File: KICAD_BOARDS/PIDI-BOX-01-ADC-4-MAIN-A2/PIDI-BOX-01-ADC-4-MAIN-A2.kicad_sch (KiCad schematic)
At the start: 87 parts, among them IC1 HCPL-354-000E, J1 Conn_01x10_Pin, J10 Conn_01x01, J2 Conn_02x03_Odd_Even, J3 Conn_02x02_Odd_Even, J4 Conn_02x01, J5 Conn_02x01, J6 CTB0709_3, J7 CTB0709_3, J8 CTB0709_2, J9 Conn_01x01, Q1 BC808, U1 AMS1117-3.3, U2 ADuM1250, U3 AMS1117CD, U4 ADS1115IDGS

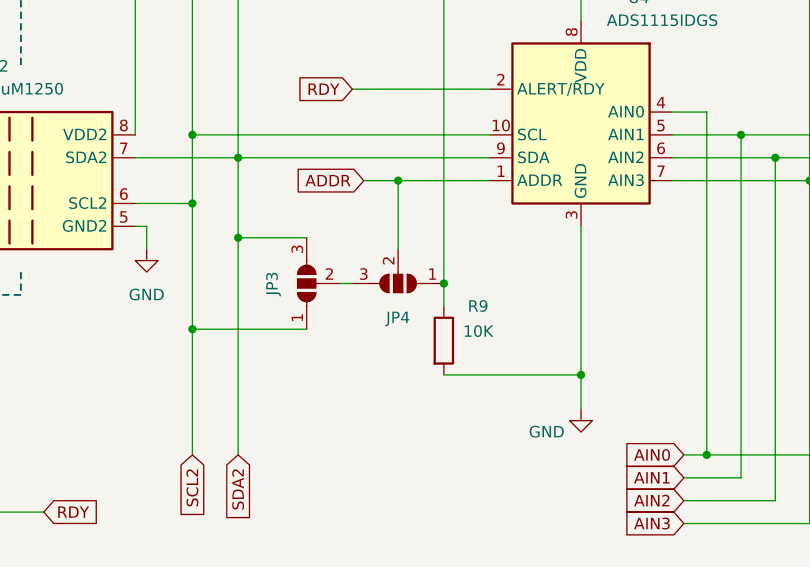
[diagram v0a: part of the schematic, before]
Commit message: ADC4 change
ADC4 Update Solderjumper 1-2 closed now
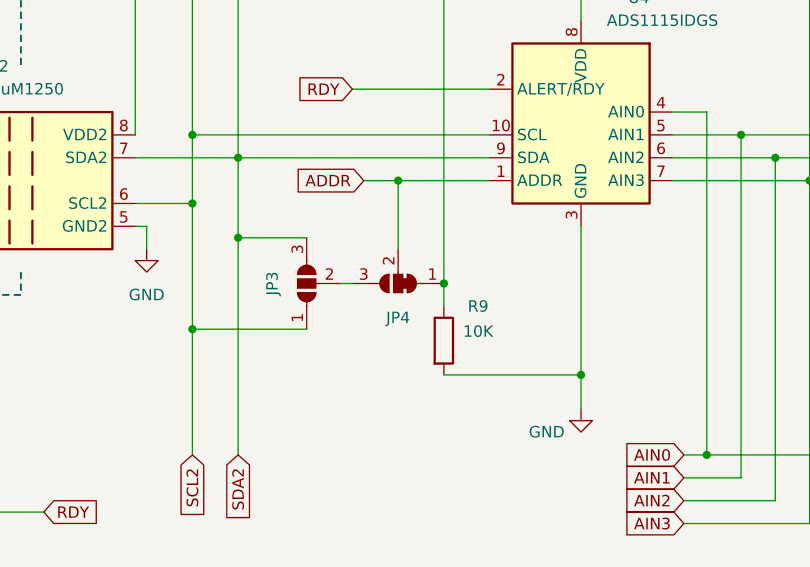
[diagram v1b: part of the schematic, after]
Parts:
- JP4: footprint Jumper:SolderJumper-3_P1.3mm_Open_RoundedPad1.0x1.5mm -> Jumper:SolderJumper-3_P1.3mm_Bridged12_Pad1.0x1.5mm; symbol Jumper:SolderJumper_3_Open -> Jumper:SolderJumper_3_Bridged12
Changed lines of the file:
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@@
 	)
 	(symbol
-		(lib_id "Jumper:SolderJumper_3_Open")
+		(lib_id "Jumper:SolderJumper_3_Bridged12")
 		(at 144.78 87.63 180)
 		(unit 1)
@@
 			)
 		)
-		(property "Footprint" "Jumper:SolderJumper-3_P1.3mm_Open_RoundedPad1.0x1.5mm"
+		(property "Footprint" "Jumper:SolderJumper-3_P1.3mm_Bridged12_Pad1.0x1.5mm"
 			(at 144.78 87.63 0)
 			(effects
@@
 			)
 		)
-		(property "Description" "Solder Jumper, 3-pole, open"
+		(property "Description" "3-pole Solder Jumper, pins 1+2 closed/bridged"
 			(at 144.78 87.63 0)
 			(effects
